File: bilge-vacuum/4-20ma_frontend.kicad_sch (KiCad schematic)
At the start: 6 parts, among them J2 Screw_Terminal_01x02, U10 MAX14626, U11 LMV321

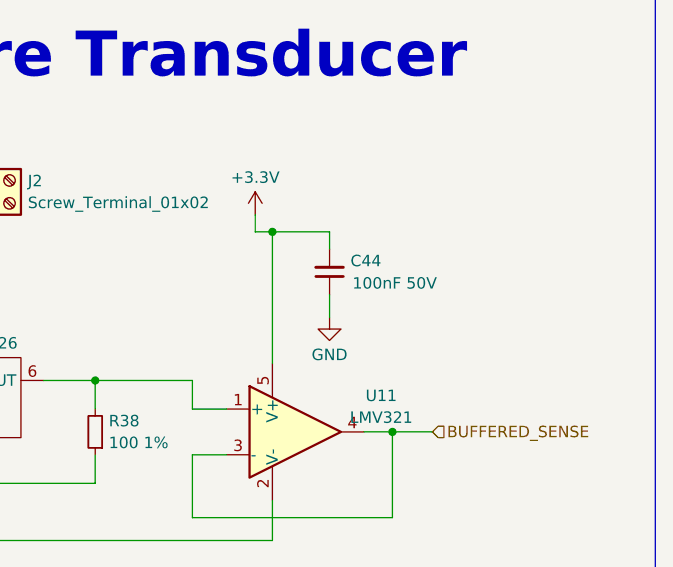
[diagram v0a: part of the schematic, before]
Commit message: Assign the bulk of parts, some passives still need custom footprints.
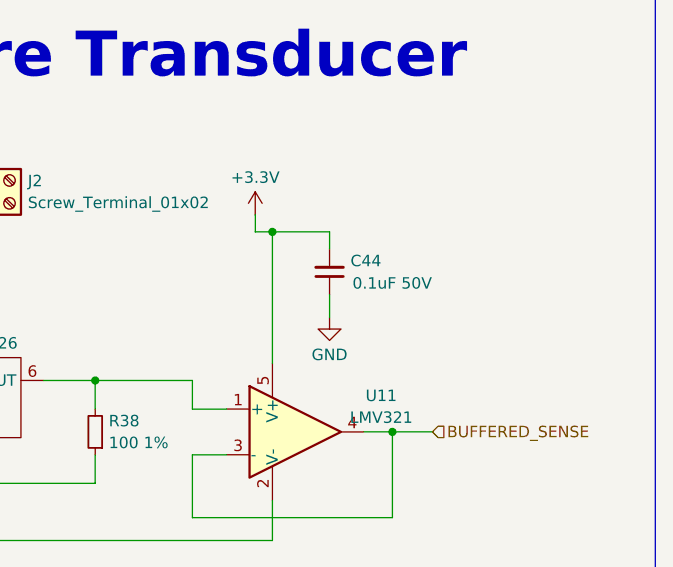
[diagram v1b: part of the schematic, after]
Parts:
- C44: value 100nF 50V -> 0.1uF 50V; footprint (none) -> Capacitor_SMD:C_0805_2012Metric
- F2: footprint (none) -> Resistor_SMD:R_2010_5025Metric
- R38: footprint (none) -> Resistor_SMD:R_0805_2012Metric
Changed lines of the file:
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@@
       (effects (font (size 1.27 1.27)) (justify right))
     )
-    (property "Footprint" "" (at 64.77 71.12 0)
+    (property "Footprint" "Resistor_SMD:R_0805_2012Metric" (at 64.77 71.12 0)
       (effects (font (size 1.27 1.27)) hide)
     )
@@
       (effects (font (size 1.27 1.27)))
     )
-    (property "Footprint" "" (at 41.91 41.91 0)
+    (property "Footprint" "Resistor_SMD:R_2010_5025Metric" (at 41.91 41.91 0)
       (effects (font (size 1.27 1.27)) (justify left) hide)
     )
@@
       (effects (font (size 1.27 1.27)) (justify right))
     )
-    (property "Value" "100nF 50V" (at 93.345 54.61 0)
+    (property "Value" "0.1uF 50V" (at 93.345 54.61 0)
       (effects (font (size 1.27 1.27)) (justify right))
     )
-    (property "Footprint" "" (at 90.805 53.34 0)
+    (property "Footprint" "Capacitor_SMD:C_0805_2012Metric" (at 90.805 53.34 0)
       (effects (font (size 1.27 1.27)) hide)
     )

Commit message: Vac progress
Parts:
- J2: footprint (none) -> Custom Parts:2604-1102
- U11: footprint (none) -> Custom Parts:SOT23-5
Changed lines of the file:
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@@
       (effects (font (size 1.27 1.27)) (justify left))
     )
-    (property "Footprint" "" (at 55.245 43.18 0)
+    (property "Footprint" "Custom Parts:2604-1102" (at 55.245 43.18 0)
       (effects (font (size 1.27 1.27)) hide)
     )
@@
       (effects (font (size 1.27 1.27)))
     )
-    (property "Footprint" "" (at 86.995 71.12 0)
+    (property "Footprint" "Custom Parts:SOT23-5" (at 86.995 71.12 0)
       (effects (font (size 1.27 1.27)) (justify left) hide)
     )

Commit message: bilge vac 1v0
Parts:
- added C44: 0.1uF 50V, Capacitor_SMD:C_0805_2012Metric, symbol Device:C_Small
- added R38: 0, Resistor_SMD:R_0805_2012Metric, symbol Device:R_Small
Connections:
- net GND: now also C44.1
- net at R38.2, U10.6 (OUT): now also R38.2; no longer U11.1 (+)
- net +3.3V renamed +3V3
- new net: C44.2, R38.1, U11.1 (+)
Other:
- moved on the sheet: C44, R38, U11

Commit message: Fixes
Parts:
- F2: footprint Resistor_SMD:R_2010_5025Metric -> Custom Parts:SMD_2016
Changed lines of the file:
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@@
       (effects (font (size 1.27 1.27)))
     )
-    (property "Footprint" "Resistor_SMD:R_2010_5025Metric" (at 41.91 41.91 0)
+    (property "Footprint" "Custom Parts:SMD_2016" (at 41.91 41.91 0)
       (effects (font (size 1.27 1.27)) (justify left) hide)
     )
